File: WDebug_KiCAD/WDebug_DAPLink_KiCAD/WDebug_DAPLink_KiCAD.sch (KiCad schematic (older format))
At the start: 37 parts, among them J1 Conn_01x04, J2 ConnDebug, J6 3.3V_Conn, P1 USB_C_Plug_USB2.0, SW1 SW_Rst, U1 XC6228D332VR-G-matrix_display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, U2 STM32F103C8Tx, Y1 8MHz

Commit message: 修改转接板接口定义
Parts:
- added R?: 0, Resistor_SMD:R_0603_1608Metric, symbol WDebug_DAPLink_KiCAD-rescue:R_Small_US-Device
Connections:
- net +3V3: now also J2.1 (Pin_1), R?.1; no longer C3.1, C5.1, C6.1, J2.10 (Pin_10), U1.5 (VOUT)
- net GND: now also J2.9 (Pin_9); no longer J2.5 (Pin_5)
- net MCU_RX1: now also J2.4 (Pin_4); no longer J2.1 (Pin_1)
- net MCU_RX2: now also J2.10 (Pin_10); no longer J2.2 (Pin_2)
- net MCU_TX1: now also J2.2 (Pin_2); no longer J2.3 (Pin_3)
- net MCU_TX2: now also J2.8 (Pin_8); no longer J2.4 (Pin_4)
- net TG_RST: now also J2.3 (Pin_3); no longer J2.7 (Pin_7)
- net T_SWCLK: now also J2.7 (Pin_7); no longer J2.9 (Pin_9)
- net T_SWDIO: now also J2.5 (Pin_5); no longer J2.8 (Pin_8)
- new net: C3.1, C5.1, C6.1, R?.2, U1.5 (VOUT)
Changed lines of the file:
@@
 Wire Wire Line
 	3200 4400 3200 4300
-Connection ~ 3500 4300
 Wire Wire Line
 	3500 4300 3500 4400
@@
 $EndComp
 Wire Wire Line
-	3500 4300 3500 4100
-Wire Wire Line
 	2750 4300 2900 4300
 Wire Wire Line
@@
 L WDebug_DAPLink_KiCAD-rescue:+3.3V-power #PWR0115
 U 1 1 5E27A434
-P 3500 4100
-F 0 "#PWR0115" H 3500 3950 50  0001 C CNN
-F 1 "+3.3V" H 3515 4273 50  0000 C CNN
-F 2 "" H 3500 4100 50  0001 C CNN
-F 3 "" H 3500 4100 50  0001 C CNN
-	1    3500 4100
+P 3950 4000
+F 0 "#PWR0115" H 3950 3850 50  0001 C CNN
+F 1 "+3.3V" H 3965 4173 50  0000 C CNN
+F 2 "" H 3950 4000 50  0001 C CNN
+F 3 "" H 3950 4000 50  0001 C CNN
+	1    3950 4000
 	1    0    0    -1
 $EndComp
@@
 L WDebug_DAPLink_KiCAD-rescue:+3.3V-power #PWR0121
 U 1 1 5E947206
-P 3850 5750
-F 0 "#PWR0121" H 3850 5600 50  0001 C CNN
-F 1 "+3.3V" H 3865 5923 50  0000 C CNN
-F 2 "" H 3850 5750 50  0001 C CNN
-F 3 "" H 3850 5750 50  0001 C CNN
-	1    3850 5750
-	1    0    0    -1
-$EndComp
-$Comp
-L WDebug_DAPLink_KiCAD-rescue:GND-power #PWR0122
-U 1 1 5E950146
-P 3150 6600
-F 0 "#PWR0122" H 3150 6350 50  0001 C CNN
-F 1 "GND" H 3155 6427 50  0000 C CNN
-F 2 "" H 3150 6600 50  0001 C CNN
-F 3 "" H 3150 6600 50  0001 C CNN
-	1    3150 6600
-	1    0    0    -1
-$EndComp
-Wire Wire Line
-	3400 5950 3850 5950
-Wire Wire Line
-	3850 5950 3850 5750
-Wire Wire Line
-	3400 6050 3850 6050
+P 2500 5750
+F 0 "#PWR0121" H 2500 5600 50  0001 C CNN
+F 1 "+3.3V" H 2515 5923 50  0000 C CNN
+F 2 "" H 2500 5750 50  0001 C CNN
+F 3 "" H 2500 5750 50  0001 C CNN
+	1    2500 5750
+	1    0    0    -1
+$EndComp
+Wire Wire Line
+	2500 5950 2500 5750
 Wire Wire Line
 	3400 6150 3850 6150
 Wire Wire Line
 	3400 6250 3850 6250
-Text Label 3850 6050 2    50   ~ 0
+Text Label 3850 6150 2    50   ~ 0
+MCU_TX2
+Text Label 3850 6250 2    50   ~ 0
 T_SWCLK
-Text Label 3850 6150 2    50   ~ 0
-T_SWDIO
-Text Label 3850 6250 2    50   ~ 0
-TG_RST
 $Comp
 L WDebug_DAPLink_KiCAD-rescue:XC6228D332VR-G-matrix_display-rescue-matrix_control_main-rescue U1
@@
 $EndComp
 Wire Wire Line
-	2900 5950 2500 5950
-Wire Wire Line
 	2900 6050 2500 6050
 Wire Wire Line
@@
 Wire Wire Line
 	2900 6250 2500 6250
-Wire Wire Line
-	2900 6350 2700 6350
-Wire Wire Line
-	3400 6350 3550 6350
-Wire Wire Line
-	3550 6350 3550 6500
-Wire Wire Line
-	3550 6500 3150 6500
-Wire Wire Line
-	3150 6500 3150 6600
-Wire Wire Line
-	2700 6500 3150 6500
-Wire Wire Line
-	2700 6350 2700 6500
-Connection ~ 3150 6500
-Text Label 2500 5950 0    50   ~ 0
+Text Label 2500 6050 0    50   ~ 0
+MCU_TX1
+Text Label 2500 6150 0    50   ~ 0
+TG_RST
+Text Label 2500 6250 0    50   ~ 0
 MCU_RX1
-Text Label 2500 6050 0    50   ~ 0
-MCU_RX2
-Text Label 2500 6150 0    50   ~ 0
-MCU_TX1
-Text Label 2500 6250 0    50   ~ 0
-MCU_TX2
 Wire Wire Line
 	1200 5600 1550 5600
 Text Label 1550 5600 2    50   ~ 0
 IF_RST
+$Comp
+L WDebug_DAPLink_KiCAD-rescue:R_Small_US-Device R?
+U 1 1 61DF4563
+P 3700 4300
+F 0 "R?" V 3650 4200 50  0000 C CNN
+F 1 "0" V 3650 4450 50  0000 C CNN
+F 2 "Resistor_SMD:R_0603_1608Metric" H 3700 4300 50  0001 C CNN
+F 3 "~" H 3700 4300 50  0001 C CNN
+	1    3700 4300
+	0    1    1    0
+$EndComp
+Wire Wire Line
+	3950 4300 3800 4300
+Wire Wire Line
+	3950 4000 3950 4300
+Wire Wire Line
+	3600 4300 3500 4300
+Connection ~ 3500 4300
+Wire Wire Line
+	2500 5950 2900 5950
+Wire Wire Line
+	2900 6350 2500 6350
+Text Label 2500 6350 0    50   ~ 0
+T_SWDIO
+$Comp
+L WDebug_DAPLink_KiCAD-rescue:GND-power #PWR0122
+U 1 1 5E950146
+P 3950 6700
+F 0 "#PWR0122" H 3950 6450 50  0001 C CNN
+F 1 "GND" H 3955 6527 50  0000 C CNN
+F 2 "" H 3950 6700 50  0001 C CNN
+F 3 "" H 3950 6700 50  0001 C CNN
+	1    3950 6700
+	1    0    0    -1
+$EndComp
+Wire Wire Line
+	3950 6050 3950 6350
+Wire Wire Line
+	3400 6050 3950 6050
+Wire Wire Line
+	3400 6350 3950 6350
+Connection ~ 3950 6350
+Wire Wire Line
+	3950 6350 3950 6700
+Wire Wire Line
+	3400 5950 3850 5950
+Text Label 3850 5950 2    50   ~ 0
+MCU_RX2
 $EndSCHEMATC

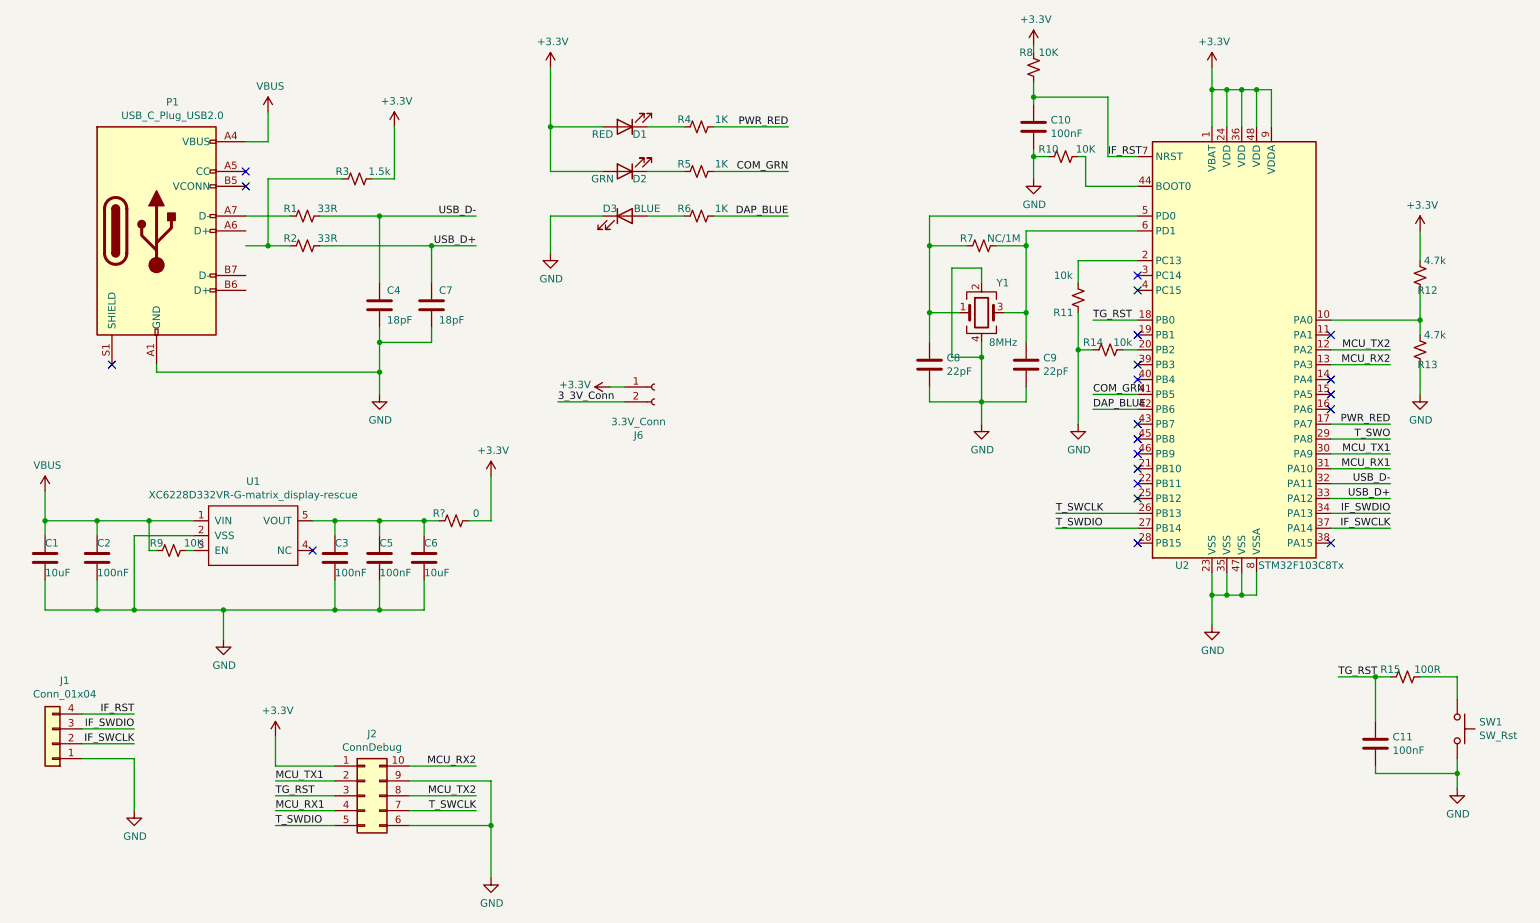
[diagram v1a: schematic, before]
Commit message: 修改V1.7版本 typec元件切换/晶振封装切换/SWD接口切换/新加3.3v调试电阻
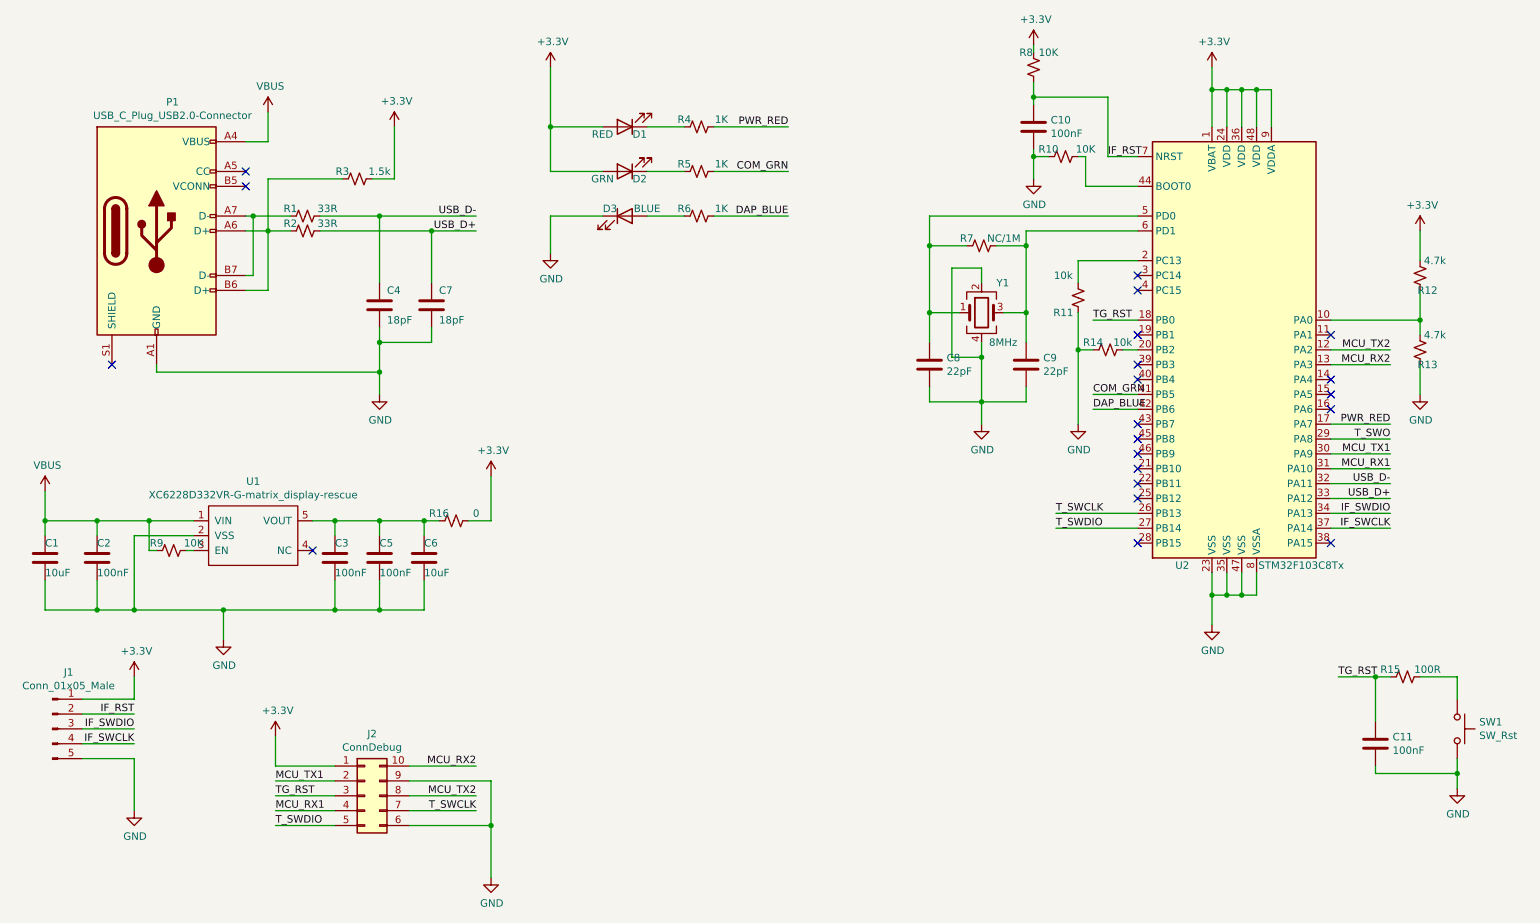
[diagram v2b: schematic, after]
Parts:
- removed J1: Conn_01x04, Connector_PinHeader_2.54mm:PinHeader_1x04_P2.54mm_Vertical, symbol WDebug_DAPLink_KiCAD-rescue:Conn_01x04-Connector_Generic
- removed J6: 3.3V_Conn, Connector_PinHeader_2.54mm:PinHeader_1x02_P2.54mm_Vertical, symbol WDebug_DAPLink_KiCAD-rescue:Conn_01x02_Female-Connector
- removed P1: USB_C_Plug_USB2.0, WDebug_DAPLink:USB-Type-C, symbol WDebug_DAPLink_KiCAD-rescue:USB_C_Plug_USB2.0-Connector
- added J1: Conn_01x05_Male, Connector_PinHeader_2.54mm:PinHeader_1x05_P2.54mm_Vertical, symbol Connector:Conn_01x05_Male
- added P1: USB_C_Plug_USB2.0-Connector, library:USB-C-SMD_KH-TYPE-C-16P, symbol WeissLib:USB_C_Plug_USB2.0-Connector
- Y1: footprint Crystal:Crystal_SMD_5032-4Pin_5.0x3.2mm -> Crystal:Crystal_SMD_3225-4Pin_3.2x2.5mm
- gave numbers to parts that had none: 1
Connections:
- net +3V3: now also J1.1 (Pin_1)
- net GND: now also J1.5 (Pin_5), P1.A1 (GND), P1.A12 (GND), P1.B1 (GND), P1.B12 (GND)
- net IF_RST: now also J1.2 (Pin_2)
- net IF_SWCLK: now also J1.4 (Pin_4)
- net IF_SWDIO: now also J1.3 (Pin_3)
- net VBUS: now also P1.A4 (VBUS), P1.A9 (VBUS), P1.B4 (VBUS), P1.B9 (VBUS)
- net at R1.2: now also P1.A7 (D-), P1.B7 (D-)
- net at R2.2, R3.2: now also P1.A6 (D+), P1.B6 (D+)
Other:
- moved on the sheet: R2
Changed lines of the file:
@@
 EESchema Schematic File Version 4
+LIBS:WDebug_DAPLink_KiCAD-cache
 EELAYER 30 0
 EELAYER END
@@
 Wire Wire Line
 	1200 5700 1550 5700
-$Comp
-L WDebug_DAPLink_KiCAD-rescue:Conn_01x04-Connector_Generic J1
-U 1 1 5E3B17F1
-P 1000 5800
-F 0 "J1" H 918 5375 50  0000 C CNN
-F 1 "Conn_01x04" H 918 5466 50  0000 C CNN
-F 2 "Connector_PinHeader_2.54mm:PinHeader_1x04_P2.54mm_Vertical" H 1000 5800 50  0001 C CNN
-F 3 "~" H 1000 5800 50  0001 C CNN
-	1    1000 5800
-	-1   0    0    1
-$EndComp
 Text Label 8100 1850 0    50   ~ 0
 IF_RST
@@
 Wire Wire Line
 	7400 2900 7550 2900
-Text Label 3850 2450 2    50   ~ 0
+Text Label 3850 2350 2    50   ~ 0
 USB_D+
 Text Label 3850 2250 2    50   ~ 0
@@
 $EndComp
 Wire Wire Line
-	3550 2450 3850 2450
-Connection ~ 3550 2450
-Wire Wire Line
-	2800 2450 3550 2450
-Wire Wire Line
-	3550 2700 3550 2450
+	3550 2350 3850 2350
+Connection ~ 3550 2350
 Wire Wire Line
 	3200 2250 3850 2250
@@
 	3200 2700 3200 2250
 Wire Wire Line
-	2450 2450 2600 2450
-Connection ~ 2450 2450
-Wire Wire Line
-	2450 2000 2450 2450
+	2450 2350 2600 2350
+Connection ~ 2450 2350
 Wire Wire Line
 	2950 2000 2450 2000
@@
 	2800 2250 3200 2250
 Wire Wire Line
-	2300 2450 2450 2450
+	2300 2350 2450 2350
 Wire Wire Line
 	2450 1750 2300 1750
@@
 	2450 1550 2450 1750
 Wire Wire Line
-	2300 2250 2600 2250
+	2300 2250 2350 2250
 $Comp
 L WDebug_DAPLink_KiCAD-rescue:VBUS-power #PWR0106
@@
 F 0 "Y1" H 7350 3100 50  0000 L CNN
 F 1 "8MHz" H 7300 2700 50  0000 L CNN
-F 2 "Crystal:Crystal_SMD_5032-4Pin_5.0x3.2mm" H 7250 2900 50  0001 C CNN
+F 2 "Crystal:Crystal_SMD_3225-4Pin_3.2x2.5mm" H 7250 2900 50  0001 C CNN
 F 3 "~" H 7250 2900 50  0001 C CNN
 	1    7250 2900
@@
 L WDebug_DAPLink_KiCAD-rescue:R_Small_US-Device R2
 U 1 1 5E0DE909
-P 2700 2450
-F 0 "R2" V 2650 2350 50  0000 C CNN
-F 1 "33R" V 2650 2600 50  0000 C CNN
-F 2 "Resistor_SMD:R_0603_1608Metric" H 2700 2450 50  0001 C CNN
-F 3 "~" H 2700 2450 50  0001 C CNN
-	1    2700 2450
+P 2700 2350
+F 0 "R2" V 2650 2250 50  0000 C CNN
+F 1 "33R" V 2650 2500 50  0000 C CNN
+F 2 "Resistor_SMD:R_0603_1608Metric" H 2700 2350 50  0001 C CNN
+F 3 "~" H 2700 2350 50  0001 C CNN
+	1    2700 2350
 	0    1    1    0
 $EndComp
@@
 	0    1    1    0
 $EndComp
-$Comp
-L WDebug_DAPLink_KiCAD-rescue:USB_C_Plug_USB2.0-Connector P1
-U 1 1 5E0DCA6A
-P 1700 2350
-F 0 "P1" H 1807 3217 50  0000 C CNN
-F 1 "USB_C_Plug_USB2.0" H 1807 3126 50  0000 C CNN
-F 2 "WDebug_DAPLink:USB-Type-C" H 1850 2350 50  0001 C CNN
-F 3 "https://www.usb.org/sites/default/files/documents/usb_type-c.zip" H 1850 2350 50  0001 C CNN
-	1    1700 2350
-	1    0    0    -1
-$EndComp
 Wire Wire Line
 	8900 1400 8800 1400
@@
 NoConn ~ 8300 4150
 NoConn ~ 2750 4500
-$Comp
-L WDebug_DAPLink_KiCAD-rescue:+3.3V-power #PWR0104
-U 1 1 5E9EB13C
-P 4750 3400
-F 0 "#PWR0104" H 4750 3250 50  0001 C CNN
-F 1 "+3.3V" V 4765 3528 50  0000 L CNN
-F 2 "" H 4750 3400 50  0001 C CNN
-F 3 "" H 4750 3400 50  0001 C CNN
-	1    4750 3400
-	0    -1   -1   0
-$EndComp
-$Comp
-L WDebug_DAPLink_KiCAD-rescue:Conn_01x02_Female-Connector J6
-U 1 1 5EBECC61
-P 5050 3400
-F 0 "J6" H 4942 3075 50  0000 C CNN
-F 1 "3.3V_Conn" H 4942 3166 50  0000 C CNN
-F 2 "Connector_PinHeader_2.54mm:PinHeader_1x02_P2.54mm_Vertical" H 5050 3400 50  0001 C CNN
-F 3 "~" H 5050 3400 50  0001 C CNN
-	1    5050 3400
-	1    0    0    -1
-$EndComp
-Wire Wire Line
-	4850 3400 4750 3400
-Wire Wire Line
-	4850 3500 4400 3500
-Text Label 4400 3500 0    50   ~ 0
-3_3V_Conn
 Wire Wire Line
 	9600 3750 10000 3750
@@
 IF_RST
 $Comp
-L WDebug_DAPLink_KiCAD-rescue:R_Small_US-Device R?
+L WDebug_DAPLink_KiCAD-rescue:R_Small_US-Device R16
 U 1 1 61DF4563
 P 3700 4300
-F 0 "R?" V 3650 4200 50  0000 C CNN
+F 0 "R16" V 3650 4200 50  0000 C CNN
 F 1 "0" V 3650 4450 50  0000 C CNN
 F 2 "Resistor_SMD:R_0603_1608Metric" H 3700 4300 50  0001 C CNN
@@
 Text Label 3850 5950 2    50   ~ 0
 MCU_RX2
+$Comp
+L Connector:Conn_01x05_Male J1
+U 1 1 61DF6B08
+P 1000 5700
+F 0 "J1" H 1108 6081 50  0000 C CNN
+F 1 "Conn_01x05_Male" H 1108 5990 50  0000 C CNN
+F 2 "Connector_PinHeader_2.54mm:PinHeader_1x05_P2.54mm_Vertical" H 1000 5700 50  0001 C CNN
+F 3 "~" H 1000 5700 50  0001 C CNN
+	1    1000 5700
+	1    0    0    -1
+$EndComp
+$Comp
+L WDebug_DAPLink_KiCAD-rescue:+3.3V-power #PWR0103
+U 1 1 61E1CDBF
+P 1550 5350
+F 0 "#PWR0103" H 1550 5200 50  0001 C CNN
+F 1 "+3.3V" H 1565 5523 50  0000 C CNN
+F 2 "" H 1550 5350 50  0001 C CNN
+F 3 "" H 1550 5350 50  0001 C CNN
+	1    1550 5350
+	1    0    0    -1
+$EndComp
+Wire Wire Line
+	1200 5500 1550 5500
+Wire Wire Line
+	1550 5500 1550 5350
+$Comp
+L WeissLib:USB_C_Plug_USB2.0-Connector P1
+U 1 1 61E3357A
+P 1700 2350
+F 0 "P1" H 1807 3217 50  0000 C CNN
+F 1 "USB_C_Plug_USB2.0-Connector" H 1807 3126 50  0000 C CNN
+F 2 "library:USB-C-SMD_KH-TYPE-C-16P" H 1850 2350 50  0001 C CNN
+F 3 "" H 1850 2350 50  0001 C CNN
+	1    1700 2350
+	1    0    0    -1
+$EndComp
+Wire Wire Line
+	2450 2000 2450 2350
+Wire Wire Line
+	2800 2350 3550 2350
+Wire Wire Line
+	3550 2350 3550 2700
+Wire Wire Line
+	2300 2650 2350 2650
+Wire Wire Line
+	2350 2650 2350 2250
+Connection ~ 2350 2250
+Wire Wire Line
+	2350 2250 2600 2250
+Wire Wire Line
+	2300 2750 2450 2750
+Wire Wire Line
+	2450 2750 2450 2350
 $EndSCHEMATC
